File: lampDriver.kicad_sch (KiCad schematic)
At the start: 61 parts, among them IC8 FAN3100TSX, Q4 BC807, T4 IMBG120R181M2HXTMA1, U1 OPA2356AIDGKR, U3 LM2902

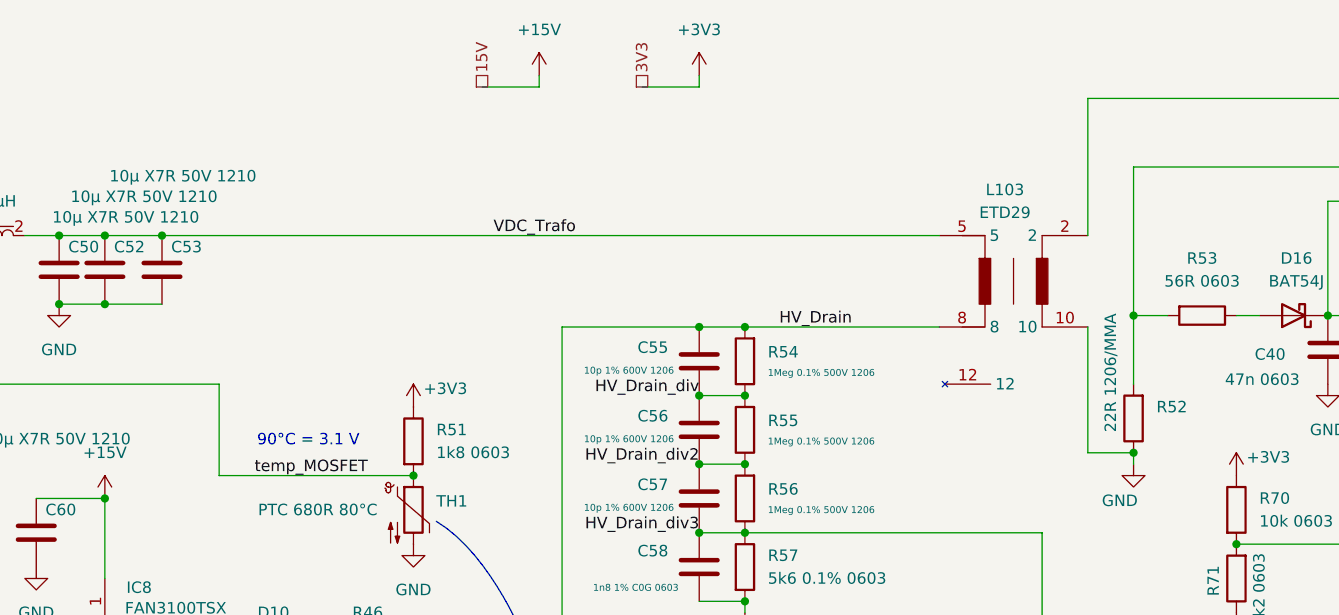
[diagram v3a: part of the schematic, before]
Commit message: added new transformer V2
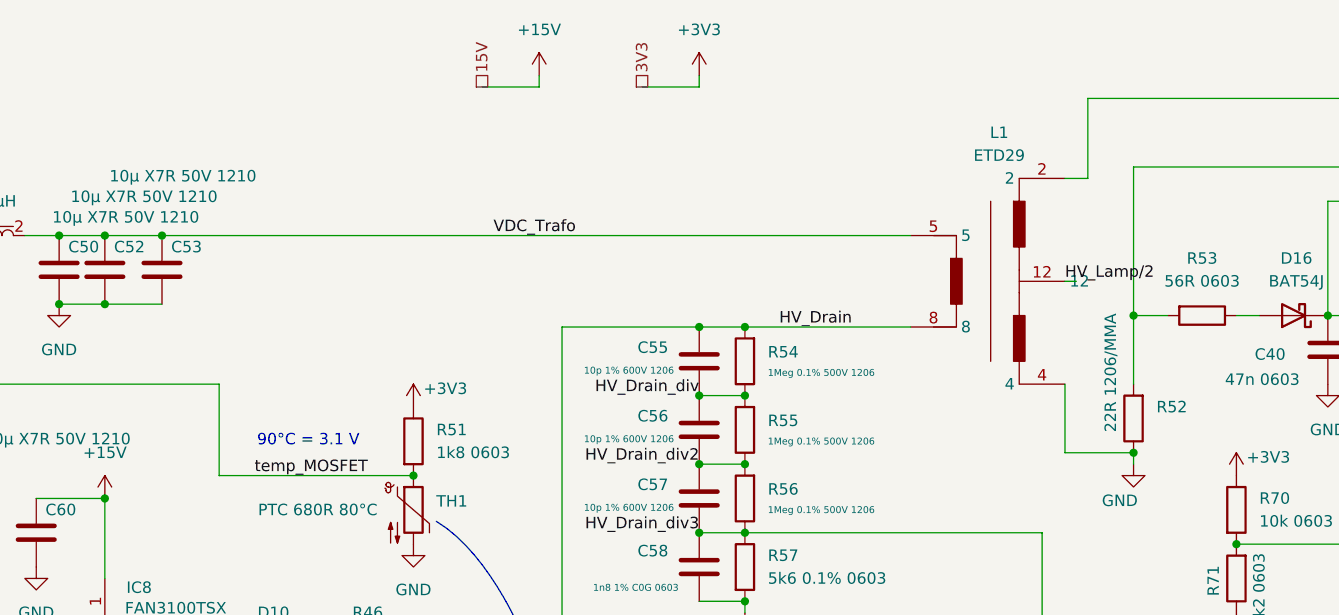
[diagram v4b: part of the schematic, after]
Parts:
- removed L103: ETD29, OSLUV:ETD29_OSLUV, symbol OSLUV:ETD29
- added L1: ETD29, OSLUV:ETD29_OSLUV_V2, symbol OSLUV:ETD29_V2
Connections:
- net GND: now also L1.4
- net HV_Drain: now also L1.8
- net Lamp_HV: now also L1.2
- net VDC_Trafo: now also L1.5
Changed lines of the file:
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@@
 	)
 	(junction
+		(at 190.5 46.99)
+		(diameter 0)
+		(color 0 0 0 0)
+	)
+	(junction
 		(at 130.81 91.44)
 		(diameter 0)
@@
 	)
 	(junction
-		(at 190.5 46.99)
-		(diameter 0)
-		(color 0 0 0 0)
-	)
-	(junction
 		(at 242.57 86.36)
 		(diameter 0)
@@
 	(wire
 		(pts
+			(xy 182.88 31.75) (xy 185.42 31.75)
+		)
+		(stroke
+			(width 0)
+			(type default)
+		)
+	)
+	(wire
+		(pts
 			(xy 130.81 91.44) (xy 132.08 91.44)
 		)
@@
 	(wire
 		(pts
+			(xy 182.88 54.61) (xy 182.88 62.23)
+		)
+		(stroke
+			(width 0)
+			(type default)
+		)
+	)
+	(wire
+		(pts
 			(xy 109.22 128.27) (xy 109.22 133.35)
 		)
@@
 	(wire
 		(pts
-			(xy 82.55 38.1) (xy 168.91 38.1)
+			(xy 82.55 38.1) (xy 165.735 38.1)
 		)
 		(stroke
@@
 	(wire
 		(pts
-			(xy 185.42 62.23) (xy 190.5 62.23)
+			(xy 182.88 62.23) (xy 190.5 62.23)
 		)
 		(stroke
@@
 	(wire
 		(pts
-			(xy 147.32 48.26) (xy 168.91 48.26)
+			(xy 147.32 48.26) (xy 165.735 48.26)
 		)
 		(stroke
@@
 	(wire
 		(pts
-			(xy 185.42 48.26) (xy 185.42 62.23)
+			(xy 76.2 67.31) (xy 76.2 76.2)
 		)
 		(stroke
@@
 	(wire
 		(pts
-			(xy 76.2 67.31) (xy 76.2 76.2)
+			(xy 182.88 43.18) (xy 184.15 43.18)
 		)
 		(stroke
@@
 	(wire
 		(pts
+			(xy 185.42 22.86) (xy 185.42 31.75)
+		)
+		(stroke
+			(width 0.254)
+			(type default)
+		)
+	)
+	(wire
+		(pts
 			(xy 121.92 133.35) (xy 170.18 133.35)
 		)
@@
 	(wire
 		(pts
-			(xy 185.42 22.86) (xy 185.42 38.1)
+			(xy 123.19 105.41) (xy 127 105.41)
 		)
 		(stroke
@@
 	(wire
 		(pts
-			(xy 123.19 105.41) (xy 127 105.41)
+			(xy 190.5 46.99) (xy 190.5 54.61)
 		)
 		(stroke
-			(width 0)
+			(width 0.254)
 			(type default)
 		)
@@
 		)
 	)
-	(wire
-		(pts
-			(xy 190.5 46.99) (xy 190.5 54.61)
-		)
-		(stroke
-			(width 0)
-			(type default)
+	(label "HV_Lamp{slash}2"
+		(at 182.88 43.18 0)
+		(effects
+			(font
+				(size 1.27 1.27)
+			)
+			(justify left bottom)
 		)
 	)
@@
 		(length 2.54)
 		(shape round)
+		(at 184.15 43.18 0)
+		(effects
+			(font
+				(size 1.27 1.27)
+			)
+			(justify left bottom)
+		)
+		(property "Net Class" "HV_Lamp/2"
+			(at 178.816 39.116 0)
+			(effects
+				(font
+					(size 1.27 1.27)
+				)
+				(justify left)
+			)
+		)
+		(property "Component Class" ""
+			(at -104.14 13.97 0)
+			(effects
+				(font
+					(size 1.27 1.27)
+					(italic yes)
+				)
+			)
+		)
+	)
+	(netclass_flag ""
+		(length 2.54)
+		(shape round)
 		(at 123.19 43.18 0)
 		(fields_autoplaced yes)
@@
 	)
 	(symbol
+		(lib_id "OSLUV:ETD29_V2")
+		(at 163.195 35.56 0)
+		(unit 1)
+		(exclude_from_sim no)
+		(in_bom yes)
+		(on_board yes)
+		(dnp no)
+		(fields_autoplaced yes)
+		(property "Reference" "L1"
+			(at 175.5775 26.67 0)
+			(effects
+				(font
+					(size 1.27 1.27)
+				)
+			)
+		)
+		(property "Value" "ETD29"
+			(at 175.5775 29.21 0)
+			(effects
+				(font
+					(size 1.27 1.27)
+				)
+			)
+		)
+		(property "Footprint" "OSLUV:ETD29_OSLUV_V2"
+			(at 182.245 130.48 0)
+			(hide yes)
+			(effects
+				(font
+					(size 1.27 1.27)
+				)
+				(justify left top)
+			)
+		)
+		(property "Datasheet" "https://product.tdk.com/system/files/dam/doc/product/ferrite/ferrite/ferrite-acc/data_sheet/80/db/fer/etd_29_16_10.pdf"
+			(at 182.245 230.48 0)
+			(hide yes)
+			(effects
+				(font
+					(size 1.27 1.27)
+				)
+				(justify left top)
+			)
+		)
+		(property "Description" "Ferrite Accessories, E Cores Accessories(EFD/ER/ETD), Coil former (ETD 29/16/10)"
+			(at 172.085 22.225 0)
+			(hide yes)
+			(effects
+				(font
+					(size 1.27 1.27)
+				)
+			)
+		)
+		(property "Height" "25"
+			(at 182.245 430.48 0)
+			(hide yes)
+			(effects
+				(font
+					(size 1.27 1.27)
+				)
+				(justify left top)
+			)
+		)
+		(property "Mouser Part Number" "871-B66359B1013T001"
+			(at 182.245 530.48 0)
+			(hide yes)
+			(effects
+				(font
+					(size 1.27 1.27)
+				)
+				(justify left top)
+			)
+		)
+		(property "Mouser Price/Stock" "https://www.mouser.co.uk/ProductDetail/EPCOS-TDK/B66359B1013T001?qs=w5o0Loj0u7PJX8yNctw%252B%252Bw%3D%3D"
+			(at 182.245 630.48 0)
+			(hide yes)
+			(effects
+				(font
+					(size 1.27 1.27)
+				)
+				(justify left top)
+			)
+		)
+		(property "Manufacturer_Name" "TDK"
+			(at 182.245 730.48 0)
+			(hide yes)
+			(effects
+				(font
+					(size 1.27 1.27)
+				)
+				(justify left top)
+			)
+		)
+		(property "Manufacturer_Part_Number" "B66359B1013T001"
+			(at 182.245 830.48 0)
+			(hide yes)
+			(effects
+				(font
+					(size 1.27 1.27)
+				)
+				(justify left top)
+			)
+		)
+		(pin "4"
+		)
+		(pin "12"
+		)
+		(pin "2"
+		)
+		(pin "8"
+		)
+		(pin "5"
+		)
+		(instances
+			(project ""
+				(path "/c6e900e0-9399-44f0-8089-9dd7b8ffe54c/9b3070c3-43e0-4d43-9da1-9bc1bd2d6fb9/8926c1e3-dcc6-4ec7-96ae-5bdb4f87d364"
+					(reference "L1")
+					(unit 1)
+				)
+			)
+		)
+	)
+	(symbol
 		(lib_id "power:GND")
 		(at 226.06 107.95 0)
@@
 					(unit 1)
 				)
-			)
-		)
-	)
-	(symbol
-		(lib_id "OSLUV:ETD29")
-		(at 166.37 35.56 0)
-		(unit 1)
-		(exclude_from_sim no)
-		(in_bom yes)
-		(on_board yes)
-		(dnp no)
-		(fields_autoplaced yes)
-		(property "Reference" "L103"
-			(at 176.2125 33.02 0)
-			(effects
-				(font
-					(size 1.27 1.27)
-				)
-			)
-		)
-		(property "Value" "ETD29"
-			(at 176.2125 35.56 0)
-			(effects
-				(font
-					(size 1.27 1.27)
-				)
-			)
-		)
-		(property "Footprint" "OSLUV:ETD29_OSLUV"
-			(at 185.42 130.48 0)
-			(hide yes)
-			(effects
-				(font
-					(size 1.27 1.27)
-				)
-				(justify left top)
-			)
-		)
-		(property "Datasheet" "https://product.tdk.com/system/files/dam/doc/product/ferrite/ferrite/ferrite-acc/data_sheet/80/db/fer/etd_29_16_10.pdf"
-			(at 185.42 230.48 0)
-			(hide yes)
-			(effects
-				(font
-					(size 1.27 1.27)
-				)
-				(justify left top)
-			)
-		)
-		(property "Description" "Ferrite Accessories, E Cores Accessories(EFD/ER/ETD), Coil former (ETD 29/16/10)"
-			(at 175.26 22.225 0)
-			(hide yes)
-			(effects
-				(font
-					(size 1.27 1.27)
-				)
-			)
-		)
-		(property "Height" "25"
-			(at 185.42 430.48 0)
-			(hide yes)
-			(effects
-				(font
-					(size 1.27 1.27)
-				)
-				(justify left top)
-			)
-		)
-		(property "Mouser Part Number" "871-B66359B1013T001"
-			(at 185.42 530.48 0)
-			(hide yes)
-			(effects
-				(font
-					(size 1.27 1.27)
-				)
-				(justify left top)
-			)
-		)
-		(property "Mouser Price/Stock" "https://www.mouser.co.uk/ProductDetail/EPCOS-TDK/B66359B1013T001?qs=w5o0Loj0u7PJX8yNctw%252B%252Bw%3D%3D"
-			(at 185.42 630.48 0)
-			(hide yes)
-			(effects
-				(font
-					(size 1.27 1.27)
-				)
-				(justify left top)
-			)
-		)
-		(property "Manufacturer_Name" "TDK"
-			(at 185.42 730.48 0)
-			(hide yes)
-			(effects
-				(font
-					(size 1.27 1.27)
-				)
-				(justify left top)
-			)
-		)
-		(property "Manufacturer_Part_Number" "B66359B1013T001"
-			(at 185.42 830.48 0)
-			(hide yes)
-			(effects
-				(font
-					(size 1.27 1.27)
-				)
-				(justify left top)
-			)
-		)
-		(pin "10"
-		)
-		(pin "5"
-		)
-		(pin "2"
-		)
-		(pin "8"
-		)
-		(pin "12"
-		)
-		(instances
-			(project ""
-				(path "/c6e900e0-9399-44f0-8089-9dd7b8ffe54c/9b3070c3-43e0-4d43-9da1-9bc1bd2d6fb9/8926c1e3-dcc6-4ec7-96ae-5bdb4f87d364"
-					(reference "L103")
-					(unit 1)
-				)

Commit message: V2 PCB
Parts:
- removed C60: 10µ X7R 50V 1210, Capacitor_SMD:C_1210_3225Metric, symbol Device:C
- removed D19: BAT54J, Diode_SMD:D_SOD-323F, symbol Diode:BAT54J
- removed IC8: FAN3100TSX, SOT95P280X145-5N, symbol Hansmann:FAN3100TSX
- removed R45: 10k 0603, Resistor_SMD:R_0603_1608Metric, symbol Device:R
- removed U3: LM2902, Package_SO:TSSOP-14_4.4x5mm_P0.65mm, symbol Amplifier_Operational:LM2902
- added C17: 100p 0603, Capacitor_SMD:C_0603_1608Metric, symbol Device:C
- added C5: 10µ X7R 50V 1210, Capacitor_SMD:C_1210_3225Metric, symbol Device:C
- added IC8: 1ED44175N01BXTSA1, SOT95P280X145-6N, symbol Hansmann:1ED44175N01BXTSA1
- added Q2: BC847, Package_TO_SOT_SMD:SOT-23, symbol Transistor_BJT:BC847
- added R29: 10k 0603, Resistor_SMD:R_0603_1608Metric, symbol Device:R
- added R77: 100k 0603, Resistor_SMD:R_0603_1608Metric, symbol Device:R
- added R79: 180R 1206/MMA, Resistor_SMD:R_1206_3216Metric, symbol Device:R
- added U3: LM2901, Package_SO:TSSOP-14_4.4x5mm_P0.65mm, symbol Comparator:LM2901
- R48, R49: value 0R47 1206 -> 0R22 1206
- R51: value 1k8 0603 -> 18k 0603
- R52: value 22R 1206/MMA -> 180R 1206/MMA
- R65, R67: value 10k 0603 -> 1k 0603
- R66: value 2k2 0603 -> 3k9 0603
- R68: value 10k 0603 -> 3k3 0603
- R69, R73: value 100k 0603 -> 10k 0603
- R71: value 2k2 0603 -> 10k 0603
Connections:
- net +15V: now also IC8.6 (VCC)
- net +3V3: now also U3.3 (V+)
- net GND: now also C17.2, C5.2, IC8.1 (OCP), IC8.2 (COM), Q2.2 (E), R77.1, R79.1, U3.12 (V-)
- net HV_Lamp/2: now also L1.12
- net Lamp_GND: now also R79.2
- net OCP: now also IC8.5 (EN/~{FLT}), Q2.3 (C), U3.1, U3.13, U3.14, U3.2
- net Usense_Lamp: now also U3.4 (-)
- net VDC_Trafo: now also C5.1
- net temp_MOSFET: now also U3.10 (-)
- net at C49.1, R44.2: now also IC8.4 (IN)
- net at Q4.3 (C), R69.2: now also R29.1
- net at R61.2, R66.2: now also R77.2, U3.5 (+)
- net at R65.1: now also U3.6 (-)
- net at R75.2, R76.2: now also U3.11 (+)
- net at D10.1 (K), R47.1: now also IC8.3 (OUT)
- net at R60.2, R62.2: now also U3.9 (+)
- net at R70.2, R71.2: now also U3.7 (+)
- net at R63.1: now also U3.8 (-)
- new net: C17.1, Q2.1 (B), R29.2
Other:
- note added: "90°C = 2.0 V"
- note removed: "90°C = 3.1 V"
- moved on the sheet: C40, C53, D10, D16, Q4, R46, R47, R52, R60, R62, R63, R67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

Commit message: Beta Prototype production data, KiCad Stable version
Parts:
- added TP10, TP11, TP12, TP13, TP14: TestPoint, TestPoint:TestPoint_Pad_D1.0mm, symbol Connector:TestPoint
- L1: footprint OSLUV:ETD29_OSLUV_V2 -> B66359B1013T001
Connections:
- net Isense_Lamp: now also TP11.1
- net Isense_MOS: now also TP13.1
- net Usense_Lamp: now also TP12.1
- net temp_MOSFET: now also TP10.1
- net at R46.2, R47.2, T4.1 (G): now also TP14.1
